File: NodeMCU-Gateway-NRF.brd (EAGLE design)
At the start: 59.7 x 40.6 mm, 32 parts, among them IC1 ATSHA204A, J2 GROVE-I2C, J3 Lipo Battery, J5 CON_HEADER_1X08-PTH, P1 PADSMALL, P2 PADNORMAL

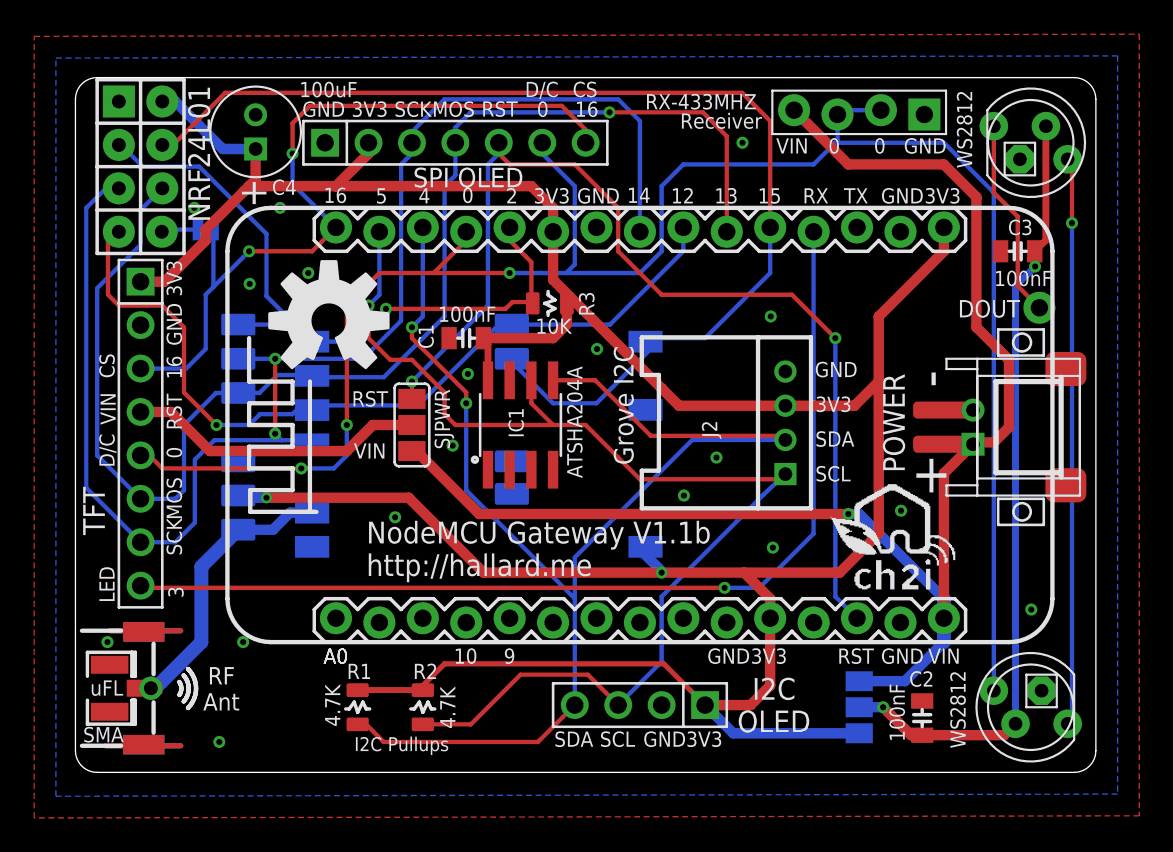
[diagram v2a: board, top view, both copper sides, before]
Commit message: Version 1.2
Added FET to protect in case of power reverse, this avoid burning
NodeMCU board
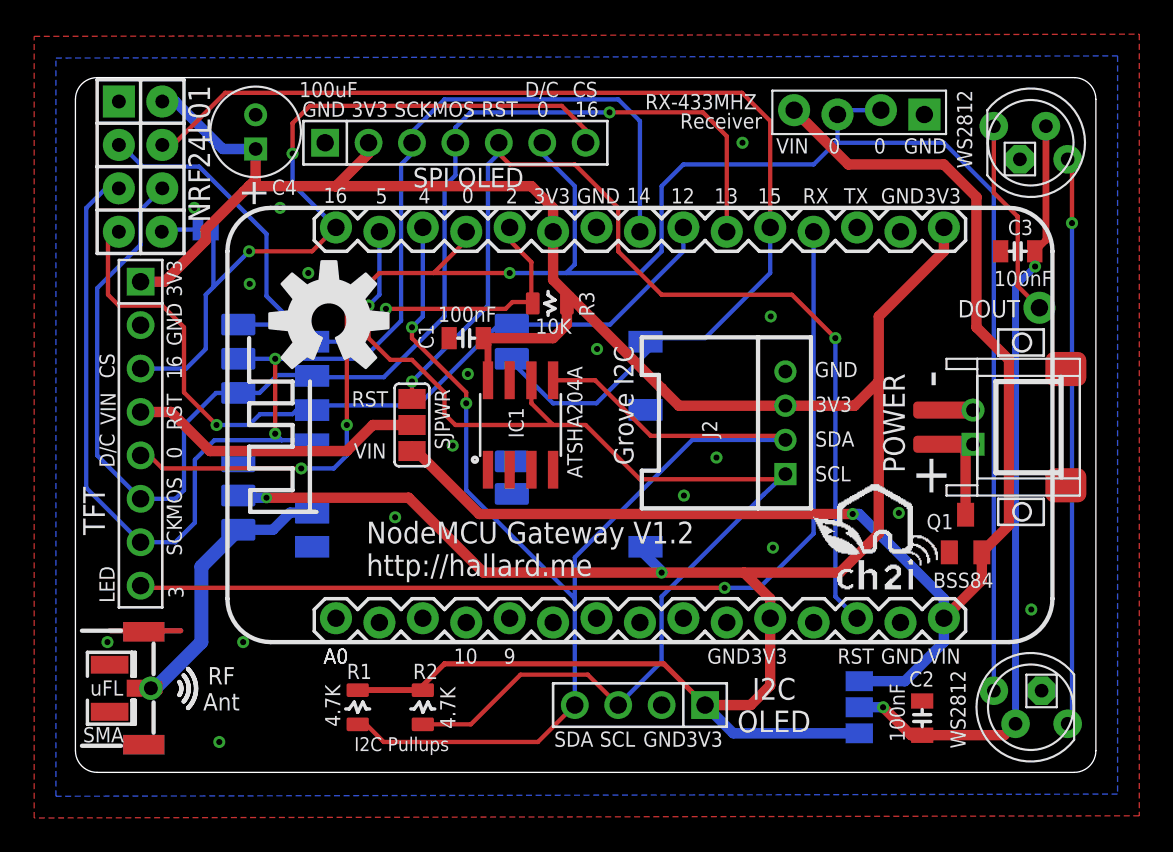
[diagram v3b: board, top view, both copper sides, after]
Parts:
- added Q1: BSS84, transistor-small-signal:SOT23
- moved U$6 1.02 mm to (47.2, 12.7)
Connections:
- new net PWR: J3.1, POWER.+, Q1.3
- net GND: now also Q1.1
- net VIN: now also Q1.2; no longer J3.1, POWER.+
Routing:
- net GND: track 17.0 -> 8.26 mm
- net PWR: track 0.00 -> 6.01 mm
- net VIN: track 85.6 -> 83.3 mm
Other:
- board text added: "NodeMCU Gateway V1.2 http://hallard.me"
- board text removed: "NodeMCU Gateway V1.1b http://hallard.me"
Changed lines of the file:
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@@
 <wire x1="58.42" y1="40.64" x2="59.69" y2="39.37" width="0" layer="20" curve="-90"/>
 <text x="38.66975" y="35.88275" size="1.27" layer="26" font="vector" ratio="15" rot="MR180">RX-Receiver</text>
-<text x="34.85975" y="14.03875" size="1.27" layer="26" font="vector" ratio="15" rot="MR180">NodeMCU Gateway V1.1b
+<text x="34.85975" y="14.03875" size="1.27" layer="26" font="vector" ratio="15" rot="MR180">NodeMCU Gateway V1.2
 http://hallard.me</text>
 <text x="29.33525" y="33.27925" size="0.889" layer="25" font="vector" ratio="15">GND</text>
@@
 <text x="22.128" y="6.35525" size="0.889" layer="25" font="vector" ratio="15">10</text>
 <text x="25.049" y="6.35525" size="0.889" layer="25" font="vector" ratio="15">9</text>
-<text x="17.01975" y="11.48825" size="1.27" layer="25" font="vector" ratio="15">NodeMCU Gateway V1.1b
+<text x="17.01975" y="11.48825" size="1.27" layer="25" font="vector" ratio="15">NodeMCU Gateway V1.2
 http://hallard.me</text>
 <text x="51.7825" y="6.48225" size="0.889" layer="26" font="vector" ratio="15" rot="MR0">VIN</text>
@@
 <attribute name="VALUE" x="6.604" y="40.1955" size="1.27" layer="25" font="vector" ratio="15" rot="R270"/>
 </element>
-<element name="U$6" library="_c2h" package="LOGO_CH2I_75MM" value="" x="48.26" y="12.7"/>
+<element name="U$6" library="_c2h" package="LOGO_CH2I_75MM" value="" x="47.244" y="12.7"/>
 <element name="U$7" library="_c2h" package="LOGO_CH2I_75MM" value="" x="21.336" y="2.794" rot="MR0"/>
 <element name="SNRFIRQ" library="SparkFun-Passives" package="PAD-JUMPER-2-NO_YES_SILK" value="NRFIRQ" x="7.62" y="31.75" smashed="yes" rot="MR180">
@@
 <attribute name="VALUE" x="16.51" y="40.386" size="0.889" layer="25" font="vector" ratio="15" rot="R180"/>
 <attribute name="NAME" x="10.668" y="36.83" size="0.254" layer="33" ratio="10" rot="R90"/>
+</element>
+<element name="Q1" library="transistor-small-signal" package="SOT23" value="BSS84" x="52.07" y="13.97" smashed="yes">
+<attribute name="NAME" x="49.784" y="14.224" size="0.889" layer="25" font="vector" ratio="15"/>
+<attribute name="VALUE" x="50.165" y="10.795" size="0.889" layer="25" font="vector" ratio="15"/>
 </element>
 </elements>
@@
 <contactref element="POWER" pad="4"/>
 <wire x1="2.032" y1="8.28675" x2="6.1595" y2="8.28675" width="0.3048" layer="1"/>
-<wire x1="1.778" y1="1.55575" x2="6.1595" y2="1.55575" width="0.3048" layer="1"/>
 <contactref element="J3" pad="2"/>
 <contactref element="J5" pad="2"/>
@@
 <contactref element="WS2812-1" pad="3"/>
 <contactref element="C3" pad="1"/>
-<via x="48.29175" y="15.3035" extent="1-16" drill="0.3556" diameter="0.7112"/>
+<via x="48.16475" y="15.1765" extent="1-16" drill="0.3556" diameter="0.7112"/>
 <via x="39.02075" y="36.83" extent="1-16" drill="0.3556" diameter="0.7112"/>
 <via x="55.91175" y="9.525" extent="1-16" drill="0.3556" diameter="0.7112"/>
 <via x="35.59175" y="16.1925" extent="1-16" drill="0.3556" diameter="0.7112"/>
 <wire x1="2.032" y1="8.28675" x2="6.1595" y2="8.28675" width="0.3048" layer="16"/>
-<wire x1="1.778" y1="1.55575" x2="6.1595" y2="1.55575" width="0.3048" layer="16"/>
 <via x="10.19175" y="28.575" extent="1-16" drill="0.3556" diameter="0.7112"/>
 <contactref element="IC1" pad="4"/>
@@
 <via x="11.96975" y="33.02" extent="1-16" drill="0.3556" diameter="0.7112"/>
 <contactref element="C4" pad="-"/>
+<contactref element="Q1" pad="1"/>
 </signal>
 <signal name="SCL">
@@
 <signal name="VIN">
 <contactref element="SJPWR" pad="1"/>
-<contactref element="JP1" pad="15"/>
-<contactref element="POWER" pad="+"/>
-<contactref element="J3" pad="1"/>
 <contactref element="RX-433MHZ" pad="+5V"/>
-<wire x1="50.8" y1="9.017" x2="50.8" y2="17.49" width="0.6096" layer="1"/>
-<wire x1="52.503" y1="19.193" x2="50.8" y2="17.49" width="0.6096" layer="1"/>
-<wire x1="52.503" y1="19.193" x2="50.8" y2="19.193" width="0.8128" layer="1"/>
-<wire x1="54.61" y1="20.193" x2="53.721" y2="19.304" width="0.6096" layer="1"/>
-<wire x1="53.721" y1="19.304" x2="52.614" y2="19.304" width="0.6096" layer="1"/>
-<wire x1="52.614" y1="19.304" x2="52.503" y2="19.193" width="0.6096" layer="1"/>
-<wire x1="50.8" y1="9.017" x2="50.8" y2="7.62" width="0.8128" layer="16"/>
 <wire x1="48.514" y1="5.334" x2="50.8" y2="7.62" width="0.6096" layer="16"/>
 <wire x1="50.8" y1="35.56" x2="45.212" y2="35.56" width="0.6096" layer="1"/>
 <wire x1="45.212" y1="35.56" x2="42.037" y2="38.735" width="0.6096" layer="1"/>
-<wire x1="54.61" y1="20.193" x2="54.61" y2="24.13" width="0.6096" layer="1"/>
 <wire x1="54.61" y1="24.13" x2="52.705" y2="26.035" width="0.6096" layer="1"/>
 <wire x1="52.705" y1="26.035" x2="52.705" y2="33.655" width="0.6096" layer="1"/>
@@
 <contactref element="SJLED" pad="1"/>
 <wire x1="45.847" y1="5.334" x2="48.514" y2="5.334" width="0.6096" layer="16"/>
-<via x="45.212" y="15.113" extent="1-16" drill="0.3556" diameter="0.7112"/>
-<wire x1="23.622" y1="15.113" x2="45.212" y2="15.113" width="0.6096" layer="1"/>
-<wire x1="45.212" y1="15.113" x2="45.847" y2="15.113" width="0.6096" layer="16"/>
+<via x="45.466" y="15.113" extent="1-16" drill="0.3556" diameter="0.7112"/>
+<wire x1="23.622" y1="15.113" x2="45.466" y2="15.113" width="0.6096" layer="1"/>
+<wire x1="45.466" y1="15.113" x2="45.847" y2="15.113" width="0.6096" layer="16"/>
 <wire x1="45.847" y1="15.113" x2="50.8" y2="10.16" width="0.6096" layer="16"/>
-<wire x1="50.8" y1="10.16" x2="50.8" y2="9.017" width="0.8128" layer="16"/>
 <wire x1="23.622" y1="15.113" x2="19.685" y2="19.05" width="0.6096" layer="1"/>
 <wire x1="19.685" y1="19.05" x2="19.685" y2="18.796" width="0.6096" layer="1"/>
+<contactref element="Q1" pad="2"/>
+<contactref element="JP1" pad="15"/>
+<wire x1="53.02" y1="12.87" x2="53.02" y2="11.237" width="0.6096" layer="1"/>
+<wire x1="53.02" y1="11.237" x2="50.8" y2="9.017" width="0.6096" layer="1"/>
+<wire x1="50.8" y1="10.16" x2="50.8" y2="9.017" width="0.6096" layer="16"/>
+<wire x1="50.8" y1="7.62" x2="50.8" y2="9.017" width="0.6096" layer="16"/>
+<wire x1="54.61" y1="24.13" x2="54.61" y2="14.46" width="0.6096" layer="1"/>
+<wire x1="54.61" y1="14.46" x2="53.02" y2="12.87" width="0.6096" layer="1"/>
 </signal>
 <signal name="N$4">
@@
 <wire x1="5.17525" y1="31.75" x2="5.04825" y2="31.623" width="0.254" layer="16"/>
 </signal>
+<signal name="PWR">
+<contactref element="Q1" pad="3"/>
+<contactref element="POWER" pad="+"/>
+<contactref element="J3" pad="1"/>
+<wire x1="52.07" y1="15.07" x2="52.07" y2="18.76" width="0.6096" layer="1"/>
+<wire x1="52.07" y1="18.76" x2="52.503" y2="19.193" width="0.6096" layer="1"/>
+<wire x1="52.503" y1="19.193" x2="50.8" y2="19.193" width="0.6096" layer="1"/>
+</signal>
 </signals>

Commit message: Bump to V1.3
* SMA/UFL Antenna connector has been size reduced
* Antenna trace and RF Module surrounded with via for better RF
isolation
* I2C OLED connector is now "lock" version, you can just plug to test it
will fit without connector
* Increased "Isolate" ground planes to avoid shorts between connectors
and ground (may happen sometimes after soldering)
* No more LED solder pad to choose VIN/3V3, added 1N4148 diode from 5V
for the 1st LED to decrease VCC to 4.4V, always works
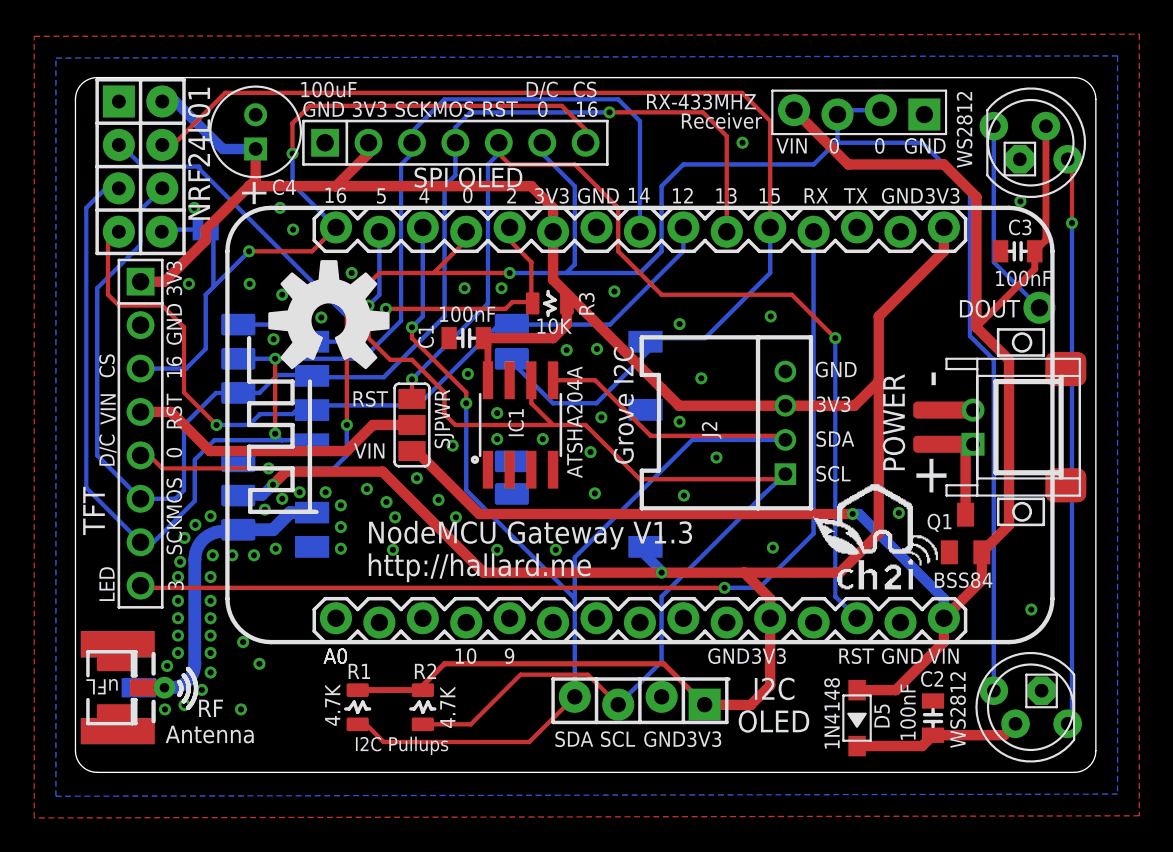
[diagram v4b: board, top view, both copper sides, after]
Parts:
- removed P1: PADSMALL, SteveMarple:PAD-SMALL
- removed SJLED: (no value), SparkFun-Passives:PAD-JUMPER-3-2OF3_NC_BY_TRACE_YES_SILK_LARGE
- removed U-FL: (no value), microbuilder:U.FL
- added D5: 1N4148, Seeed-Discrete:SOD123-2.7X1.6
- added J$2: ANTENNATINY, _c2h:SMA_UFL_PAD_TINY
- I2C_OLED: value CON_HEADER_1X04'SMALL'' -> CON_HEADER_1X04'LOCK'; device _c2h:M1X4 -> _c2h:1X04_LOCK
- moved I2C_OLED 5.27 mm to (38.1, 5.33)
- moved C2 0.63 mm to (50.2, 3.17)
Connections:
- net 3V3: no longer SJLED.3
- net ANT: now also J$2.ANT1, J$2.ANT2, J$2.ANT3; no longer P1.1, U-FL.3
- net GND: now also J$2.GND1, J$2.GND2, J$2.GND3, J$2.GND4; no longer U-FL.1, U-FL.2
- net VIN: now also C3.2, D5.1, WS2812-1.2; no longer SJLED.1
- net VLED: now also D5.2; no longer C3.2, SJLED.2, WS2812-1.2
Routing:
- net VLED: track 45.8 -> 9.81 mm, vias 2 -> 0
- net VIN: track 83.3 -> 97.1 mm
- net 3V3: track 186.0 -> 177.5 mm
- net GND: track 8.26 -> 2.24 mm, vias 18 -> 75
- net ANT: track 22.3 -> 19.8 mm
- net GPIO2: track 40.3 -> 42.4 mm
- net GPIO0: track 112.0 -> 111.2 mm
- net SCK: track 87.4 -> 86.7 mm
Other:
- board text added: "NodeMCU Gateway V1.3 http://hallard.me"
- board text added: "RF Antenna"
- board text removed: "NodeMCU Gateway V1.2 http://hallard.me"
- board text removed: "RF Ant"
- board text removed: "SMA"
- board text removed: "uFL"
